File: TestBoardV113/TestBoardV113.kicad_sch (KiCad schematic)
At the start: 97 parts, among them J1 Conn_01x02_Socket, J10 Conn_01x02_Pin, J11 Conn_01x02_Pin, J12 Conn_01x02_Pin, J13 Conn_02x03_Odd_Even, J14 Conn_02x03_Odd_Even, J15 Conn_01x02_Pin, J16 Conn_02x03_Odd_Even, J17 Conn_01x01_Pin, J18 Conn_01x28_Socket, J19 Conn_01x01_Pin, J2 Conn_02x06_Odd_Even, J20 Conn_01x01_Pin, J21 Conn_01x28_Socket, J22 Conn_01x02_Pin, J23 Conn_01x02_Socket, J24 Conn_01x01_Pin, J25 Conn_01x02_Pin, J26 Conn_01x02_Pin, J27 Conn_02x03_Odd_Even, J28 Conn_01x02_Socket, J3 Conn_01x02_Pin, J4 Conn_01x02_Pin, J5 Conn_01x02_Pin, J6 Conn_01x02_Pin, J7 Conn_01x03_Pin, J8 Conn_01x03_Pin, J9 Conn_01x03_Pin, SW1 SW_DIP_x07, U3 NCP705MTADJTCG, U4 TAR5SxxU_SOT353F, U5 TXB0104PW, U6 TXB0104PW

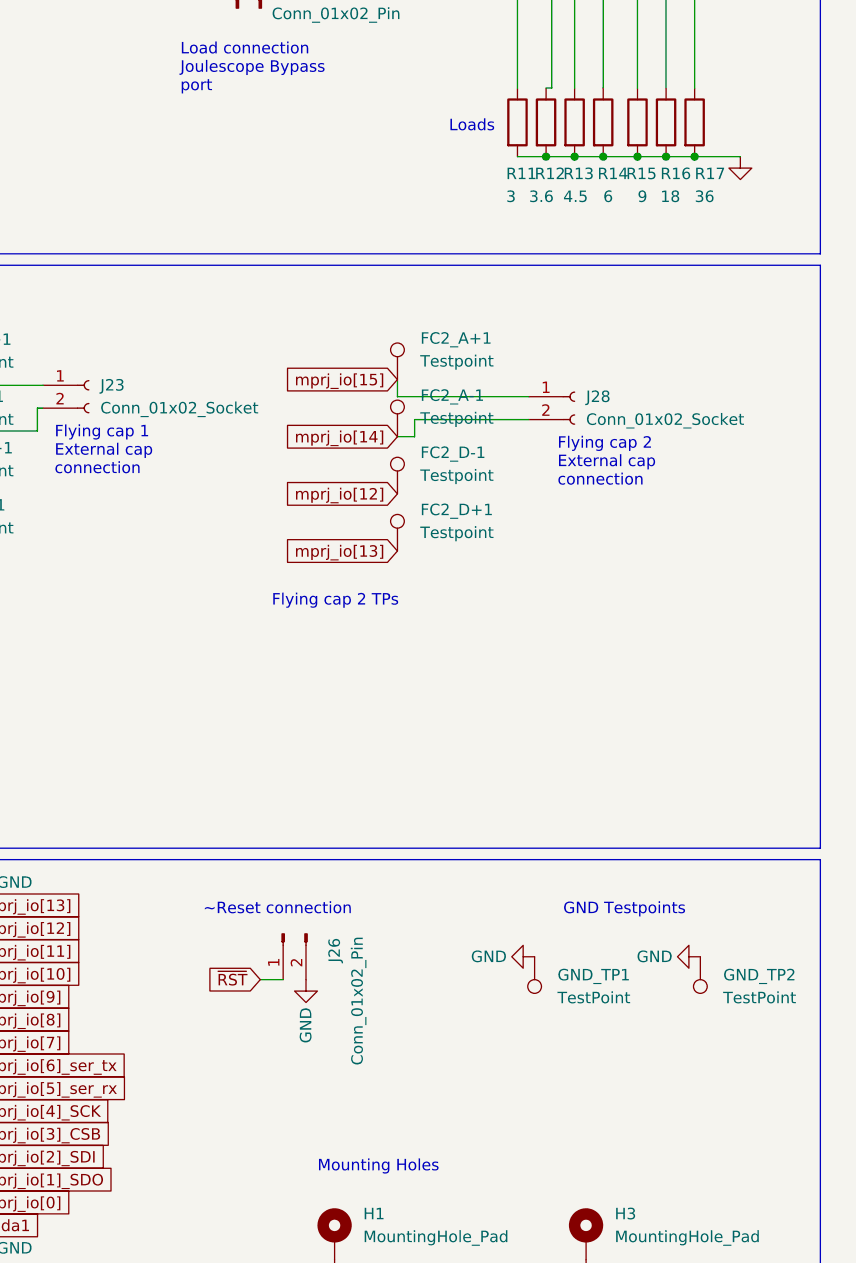
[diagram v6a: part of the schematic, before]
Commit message: pull up for ~reset
Added pull-up resistor (100K) for ~Reset
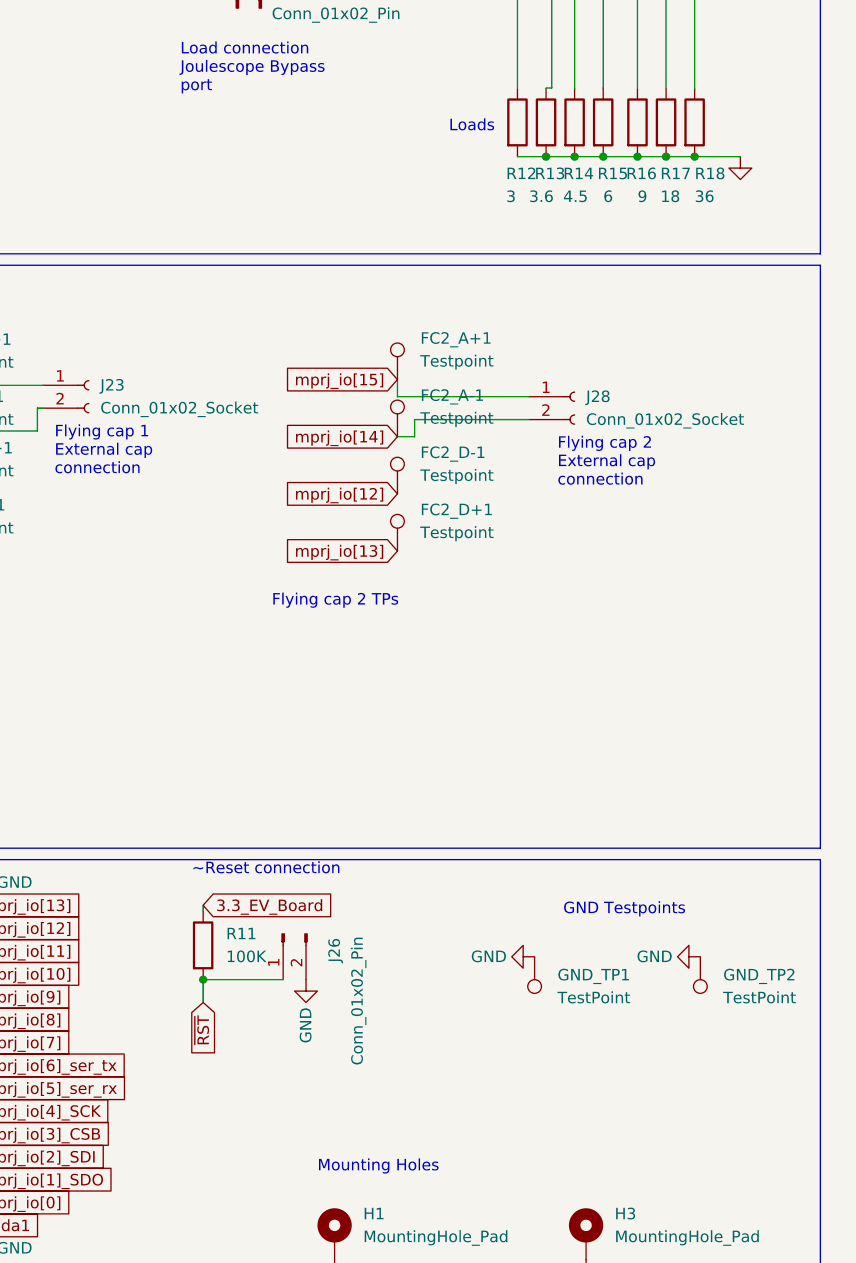
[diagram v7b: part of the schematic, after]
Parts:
- added R11: 100K, Resistor_SMD:R_0805_2012Metric, symbol Device:R
- renumbered R11 to R12, R12 to R13, R13 to R14, R14 to R15, R15 to R16, R16 to R17, R17 to R18
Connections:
- net 3.3_EV_Board: now also R11.1
- net ~{RST}: now also R11.2
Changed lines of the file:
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@@
   (junction (at 73.66 63.5) (diameter 0) (color 0 0 0 0)
   )
+  (junction (at 318.77 177.165) (diameter 0) (color 0 0 0 0)
+  )
   (junction (at 64.77 28.575) (diameter 0) (color 0 0 0 0)
   )
@@
     (stroke (width 0) (type default))
   )
+  (wire (pts (xy 318.77 168.91) (xy 318.77 169.545))
+    (stroke (width 0) (type default))
+  )
   (wire (pts (xy 354.965 114.935) (xy 342.265 114.935))
     (stroke (width 0) (type default))
@@
     (stroke (width 0) (type default))
   )
+  (wire (pts (xy 318.77 177.165) (xy 327.66 177.165))
+    (stroke (width 0) (type default))
+  )
   (wire (pts (xy 49.53 190.5) (xy 52.07 190.5))
     (stroke (width 0) (type default))
@@
     (stroke (width 0) (type default))
   )
-  (wire (pts (xy 325.12 177.165) (xy 327.66 177.165))
+  (wire (pts (xy 318.77 179.705) (xy 318.77 177.165))
     (stroke (width 0) (type default))
   )
@@
     (effects (font (size 1.27 1.27)) (justify left bottom))
   )
-  (text "~Reset connection" (at 318.77 170.18 0)
+  (text "~Reset connection" (at 317.5 165.735 0)
     (effects (font (size 1.27 1.27)) (justify left bottom))
   )
@@
     )
   )
+  (global_label "3.3_EV_Board" (shape input) (at 318.77 168.91 0) (fields_autoplaced)
+    (effects (font (size 1.27 1.27)) (justify left))
+    (property "Intersheetrefs" "${INTERSHEET_REFS}" (at 334.455 168.91 0)
+      (effects (font (size 1.27 1.27)) (justify left) hide)
+    )
+  )
   (global_label "~{RST}" (shape input) (at 250.19 176.53 180) (fields_autoplaced)
     (effects (font (size 1.27 1.27)) (justify right))
@@
     )
   )
-  (global_label "~{RST}" (shape input) (at 325.12 177.165 180) (fields_autoplaced)
+  (global_label "~{RST}" (shape input) (at 318.77 179.705 270) (fields_autoplaced)
     (effects (font (size 1.27 1.27)) (justify right))
-    (property "Intersheetrefs" "${INTERSHEET_REFS}" (at 707.39 280.035 0)
-      (effects (font (size 1.27 1.27)) hide)
+    (property "Intersheetrefs" "${INTERSHEET_REFS}" (at 318.77 186.1373 90)
+      (effects (font (size 1.27 1.27)) (justify right) hide)
     )
   )
@@
   (symbol (lib_id "Device:R") (at 363.22 81.915 0) (unit 1)
     (in_bom yes) (on_board yes) (dnp no)
-    (property "Reference" "R14" (at 362.585 87.63 0)
+    (property "Reference" "R15" (at 362.585 87.63 0)
       (effects (font (size 1.27 1.27)) (justify left))
     )
@@
       (project "TestBoardV113"
         (path "/4de6d057-85e0-4efd-8c0f-256b0c8a5cf9"
-          (reference "R14") (unit 1)
+          (reference "R15") (unit 1)
         )
       )
@@
   (symbol (lib_id "Device:R") (at 370.205 81.915 0) (unit 1)
     (in_bom yes) (on_board yes) (dnp no)
-    (property "Reference" "R16" (at 369.57 87.63 0)
+    (property "Reference" "R17" (at 369.57 87.63 0)
       (effects (font (size 1.27 1.27)) (justify left))
     )
@@
       (project "TestBoardV113"
         (path "/4de6d057-85e0-4efd-8c0f-256b0c8a5cf9"
-          (reference "R16") (unit 1)
+          (reference "R17") (unit 1)
         )
       )
@@
   (symbol (lib_id "Device:R") (at 356.87 81.915 0) (unit 1)
     (in_bom yes) (on_board yes) (dnp no)
-    (property "Reference" "R12" (at 355.6 87.63 0)
+    (property "Reference" "R13" (at 355.6 87.63 0)
       (effects (font (size 1.27 1.27)) (justify left))
     )
@@
       (project "TestBoardV113"
         (path "/4de6d057-85e0-4efd-8c0f-256b0c8a5cf9"
-          (reference "R12") (unit 1)
+          (reference "R13") (unit 1)
         )
       )
@@
   (symbol (lib_id "Device:R") (at 353.695 81.915 0) (unit 1)
     (in_bom yes) (on_board yes) (dnp no)
-    (property "Reference" "R11" (at 352.425 87.63 0)
+    (property "Reference" "R12" (at 352.425 87.63 0)
       (effects (font (size 1.27 1.27)) (justify left))
     )
@@
       (project "TestBoardV113"
         (path "/4de6d057-85e0-4efd-8c0f-256b0c8a5cf9"
-          (reference "R11") (unit 1)
+          (reference "R12") (unit 1)
         )
       )
@@
   (symbol (lib_id "Device:R") (at 373.38 81.915 0) (unit 1)
     (in_bom yes) (on_board yes) (dnp no)
-    (property "Reference" "R17" (at 373.38 87.63 0)
+    (property "Reference" "R18" (at 373.38 87.63 0)
       (effects (font (size 1.27 1.27)) (justify left))
     )
@@
       (project "TestBoardV113"
         (path "/4de6d057-85e0-4efd-8c0f-256b0c8a5cf9"
-          (reference "R17") (unit 1)
+          (reference "R18") (unit 1)
         )
       )
@@
   (symbol (lib_id "Device:R") (at 367.03 81.915 0) (unit 1)
     (in_bom yes) (on_board yes) (dnp no)
-    (property "Reference" "R15" (at 365.76 87.63 0)
+    (property "Reference" "R16" (at 365.76 87.63 0)
       (effects (font (size 1.27 1.27)) (justify left))
     )
@@
       (project "TestBoardV113"
         (path "/4de6d057-85e0-4efd-8c0f-256b0c8a5cf9"
-          (reference "R15") (unit 1)
+          (reference "R16") (unit 1)
         )
       )
@@
     )
   )
+  (symbol (lib_id "Device:R") (at 318.77 173.355 0) (unit 1)
+    (in_bom yes) (on_board yes) (dnp no) (fields_autoplaced)
+    (property "Reference" "R11" (at 321.31 172.085 0)
+      (effects (font (size 1.27 1.27)) (justify left))
+    )
+    (property "Value" "100K" (at 321.31 174.625 0)
+      (effects (font (size 1.27 1.27)) (justify left))
+    )
+    (property "Footprint" "Resistor_SMD:R_0805_2012Metric" (at 316.992 173.355 90)
+      (effects (font (size 1.27 1.27)) hide)
+    )
+    (property "Datasheet" "~" (at 318.77 173.355 0)
+      (effects (font (size 1.27 1.27)) hide)
+    )
+    (pin "1")
+    (pin "2")
+    (instances
+      (project "TestBoardV113"
+        (path "/4de6d057-85e0-4efd-8c0f-256b0c8a5cf9"
+          (reference "R11") (unit 1)
+        )
+      )
+    )
+  )
   (symbol (lib_id "Connector:TestPoint") (at 29.845 240.665 90) (unit 1)
     (in_bom yes) (on_board yes) (dnp no) (fields_autoplaced)
@@
   (symbol (lib_id "Device:R") (at 360.045 81.915 0) (unit 1)
     (in_bom yes) (on_board yes) (dnp no)
-    (property "Reference" "R13" (at 358.775 87.63 0)
+    (property "Reference" "R14" (at 358.775 87.63 0)
       (effects (font (size 1.27 1.27)) (justify left))
     )
@@
       (project "TestBoardV113"
         (path "/4de6d057-85e0-4efd-8c0f-256b0c8a5cf9"
-          (reference "R13") (unit 1)
+          (reference "R14") (unit 1)
         )
       )

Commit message: Changed some names
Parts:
- FC1_A+1, FC1_A-1, FC1_D+1, FC1_D-1, FC2_A+1, FC2_A-1, FC2_D+1, FC2_D-1, Vout1_NF1, Vout2_NF1, Vout_F1, Vout_Load1: value Testpoint -> TestPoint
- U1, U2: value ~ -> NCP705MTADJTCG
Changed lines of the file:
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@@
   (symbol (lib_id "Connector:TestPoint") (at 271.78 21.59 0) (unit 1)
     (in_bom yes) (on_board yes) (dnp no) (fields_autoplaced)
-    (property "Reference" "Vout1_NF1" (at 274.32 18.288 0)
-      (effects (font (size 1.27 1.27)) (justify left))
-    )
-    (property "Value" "Testpoint" (at 274.32 19.558 0)
+    (property "Reference" "Vout1_NF1" (at 274.32 17.018 0)
+      (effects (font (size 1.27 1.27)) (justify left))
+    )
+    (property "Value" "TestPoint" (at 274.32 19.558 0)
       (effects (font (size 1.27 1.27)) (justify left))
     )
@@
       (effects (font (size 1.27 1.27)))
     )
-    (property "Value" "~" (at 87.63 64.77 0)
+    (property "Value" "NCP705MTADJTCG" (at 87.63 64.77 0)
       (effects (font (size 1.27 1.27)))
     )
@@
       (effects (font (size 1.27 1.27)) (justify left))
     )
-    (property "Value" "Testpoint" (at 289.56 120.65 0)
+    (property "Value" "TestPoint" (at 289.56 120.65 0)
       (effects (font (size 1.27 1.27)) (justify left))
     )
@@
       (effects (font (size 1.27 1.27)) (justify left))
     )
-    (property "Value" "Testpoint" (at 289.56 127 0)
+    (property "Value" "TestPoint" (at 289.56 127 0)
       (effects (font (size 1.27 1.27)) (justify left))
     )
@@
       (effects (font (size 1.27 1.27)) (justify right))
     )
-    (property "Value" "Testpoint" (at 274.32 80.772 0)
+    (property "Value" "TestPoint" (at 274.32 80.772 0)
       (effects (font (size 1.27 1.27)) (justify right))
     )
@@
       (effects (font (size 1.27 1.27)))
     )
-    (property "Value" "~" (at 87.63 29.845 0)
+    (property "Value" "NCP705MTADJTCG" (at 87.63 29.845 0)
       (effects (font (size 1.27 1.27)))
     )
@@
       (effects (font (size 1.27 1.27)) (justify left))
     )
-    (property "Value" "Testpoint" (at 289.56 108.585 0)
+    (property "Value" "TestPoint" (at 289.56 108.585 0)
       (effects (font (size 1.27 1.27)) (justify left))
     )
@@
       (effects (font (size 1.27 1.27)) (justify left))
     )
-    (property "Value" "Testpoint" (at 342.9 108.458 0)
+    (property "Value" "TestPoint" (at 342.9 108.458 0)
       (effects (font (size 1.27 1.27)) (justify left))
     )
@@
       (effects (font (size 1.27 1.27)) (justify left))
     )
-    (property "Value" "Testpoint" (at 352.933 33.401 0)
+    (property "Value" "TestPoint" (at 352.933 33.401 0)
       (effects (font (size 1.27 1.27)) (justify left))
     )
@@
       (effects (font (size 1.27 1.27)) (justify left))
     )
-    (property "Value" "Testpoint" (at 289.56 114.935 0)
+    (property "Value" "TestPoint" (at 289.56 114.935 0)
       (effects (font (size 1.27 1.27)) (justify left))
     )
@@
       (effects (font (size 1.27 1.27)) (justify left))
     )
-    (property "Value" "Testpoint" (at 299.72 31.75 0)
+    (property "Value" "TestPoint" (at 299.72 31.75 0)
       (effects (font (size 1.27 1.27)) (justify left))
     )
@@
       (effects (font (size 1.27 1.27)) (justify left))
     )
-    (property "Value" "Testpoint" (at 342.9 127.508 0)
+    (property "Value" "TestPoint" (at 342.9 127.508 0)
       (effects (font (size 1.27 1.27)) (justify left))
     )
@@
       (effects (font (size 1.27 1.27)) (justify left))
     )
-    (property "Value" "Testpoint" (at 342.9 121.158 0)
+    (property "Value" "TestPoint" (at 342.9 121.158 0)
       (effects (font (size 1.27 1.27)) (justify left))
     )
@@
       (effects (font (size 1.27 1.27)) (justify left))
     )
-    (property "Value" "Testpoint" (at 342.9 114.808 0)
-      (effects (font (size 1.27 1.27)) (justify left))
-    )
+    (property "Value" "TestPoint" (at 342.9 114.808 0)
+      (effects (font (size 1.27 1.27)) (justify left))
+    )
